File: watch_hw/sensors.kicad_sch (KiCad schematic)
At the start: 4 parts, among them J2 FH19C-7S-0.5SH, U7 BMA456

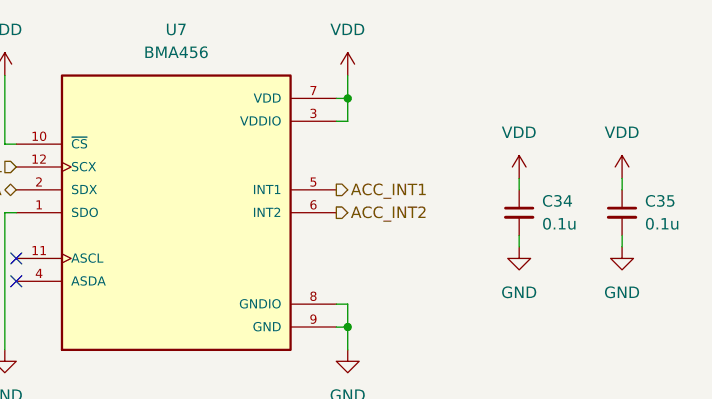
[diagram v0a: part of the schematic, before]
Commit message: Finalize (?) part selection, start layout
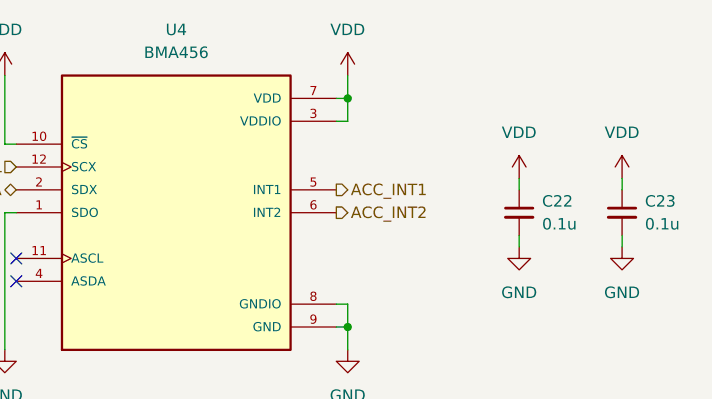
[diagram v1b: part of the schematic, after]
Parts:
- renumbered C34 to C22, C35 to C23, U7 to U4

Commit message: Routing progress
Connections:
- net HR_GPIO: no longer names the net of J2.3 (Pin_3)
- net HR_LDO_EN: no longer names the net of J2.4 (Pin_4)
- no-connect marks 2 -> 4
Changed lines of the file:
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@@
   (junction (at 220.98 107.95) (diameter 0) (color 0 0 0 0)
   )
+  (no_connect (at 81.28 92.71))
   (no_connect (at 184.15 100.33))
   (no_connect (at 184.15 102.87))
+  (no_connect (at 81.28 90.17))
   (wire (pts (xy 219.71 82.55) (xy 220.98 82.55))
     (stroke (width 0) (type default))
@@
     (effects (font (size 1.27 1.27)) (justify right))
   )
-  (hierarchical_label "HR_GPIO" (shape bidirectional) (at 81.28 90.17 180) (fields_autoplaced)
-    (effects (font (size 1.27 1.27)) (justify right))
-  )
   (hierarchical_label "HR_INT" (shape output) (at 81.28 87.63 180) (fields_autoplaced)
     (effects (font (size 1.27 1.27)) (justify right))
@@
     (effects (font (size 1.27 1.27)) (justify right))
   )
-  (hierarchical_label "HR_LDO_EN" (shape input) (at 81.28 92.71 180) (fields_autoplaced)
-    (effects (font (size 1.27 1.27)) (justify right))
-  )

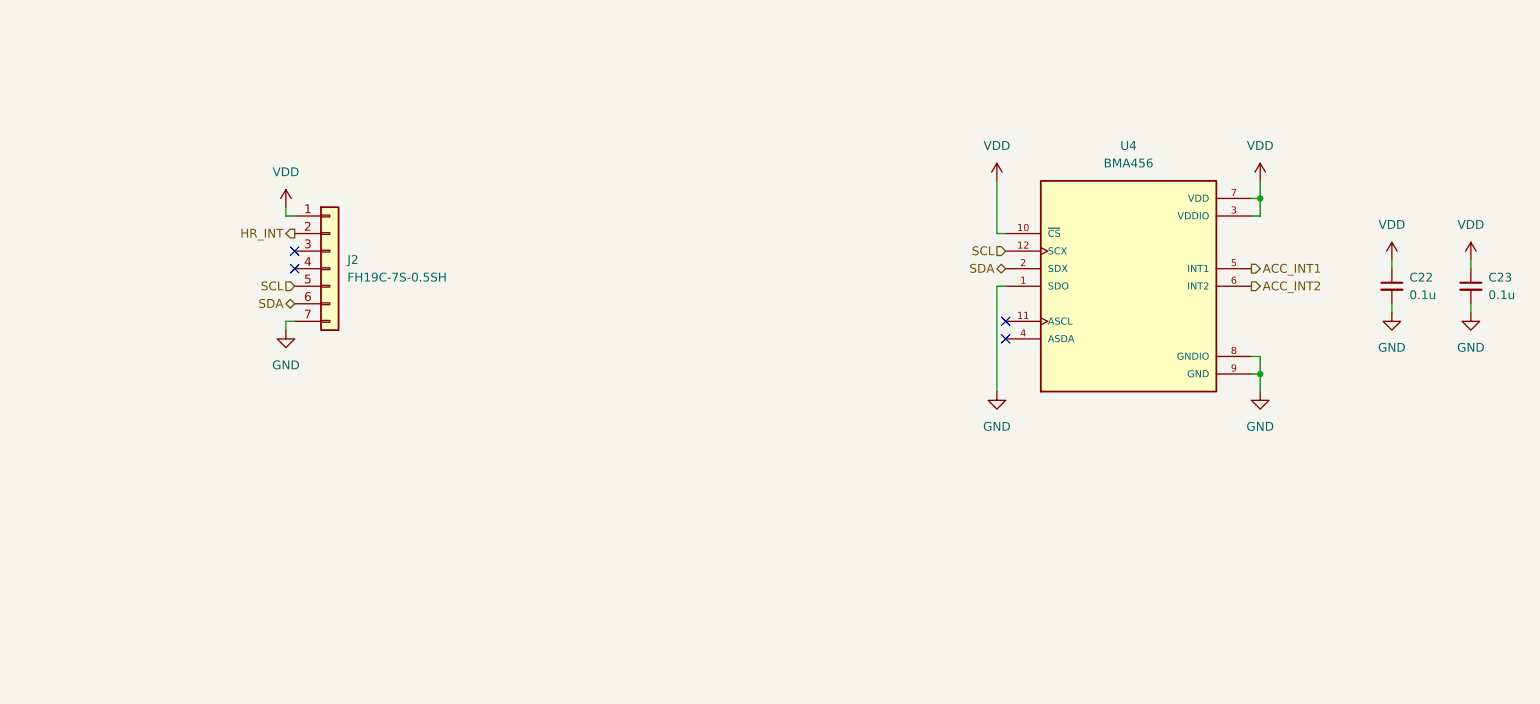
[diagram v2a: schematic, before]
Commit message: Clean up library symbols, update to kicad 8
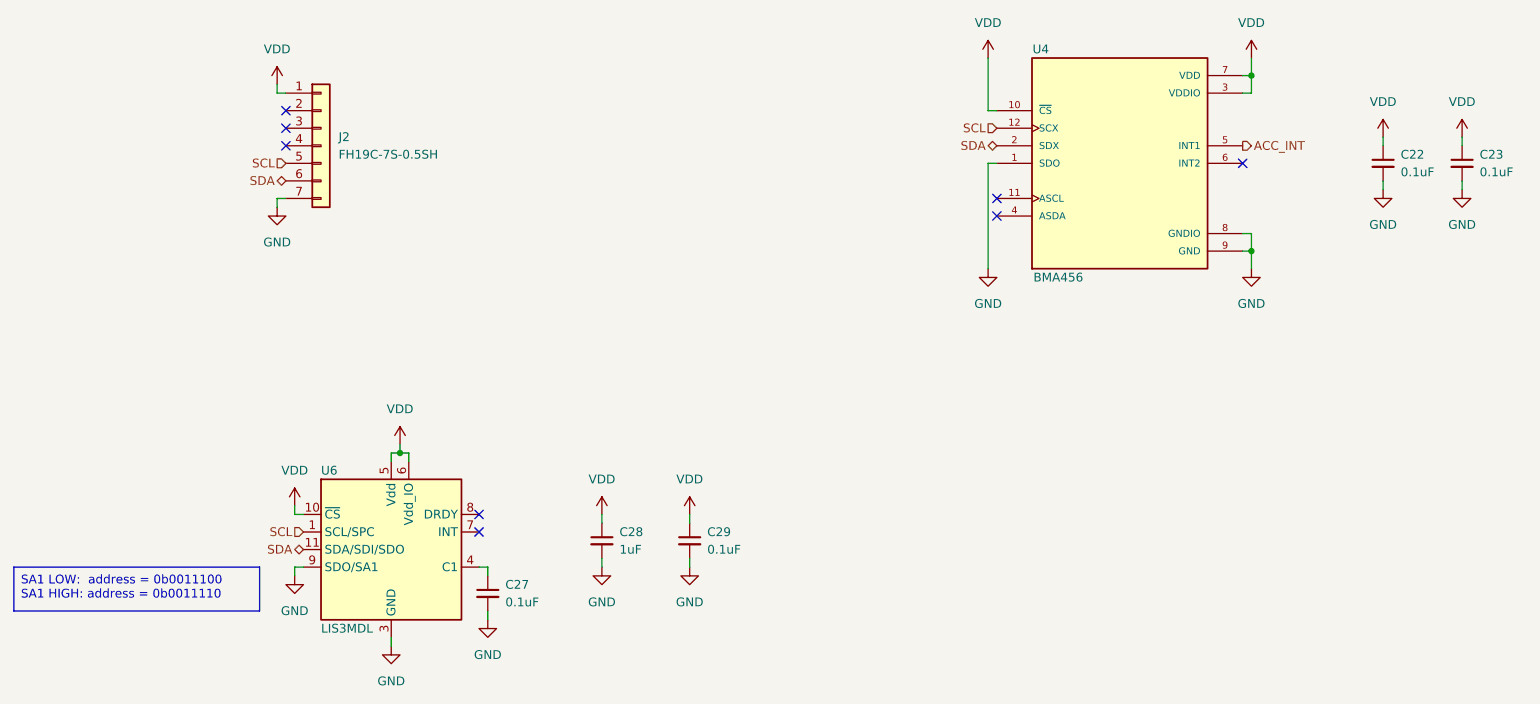
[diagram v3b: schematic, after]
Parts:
- added C27, C29: 0.1uF, Capacitor_SMD:C_0402_1005Metric_Pad0.74x0.62mm_HandSolder, symbol Device:C_Small
- added C28: 1uF, Capacitor_SMD:C_0402_1005Metric_Pad0.74x0.62mm_HandSolder, symbol Device:C_Small
- added U6: LIS3MDL, watch:LIS3MDLTR, symbol Sensor_Magnetic:LIS3MDL
- C22, C23: value 0.1u -> 0.1uF
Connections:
- net GND: now also C27.2, C28.2, C29.2, U6.12 (GND), U6.2 (GND), U6.3 (GND), U6.9 (SDO/SA1)
- net SCL: now also U6.1 (SCL/SPC)
- net SDA: now also U6.11 (SDA/SDI/SDO)
- net VDD: now also C28.1, C29.1, U6.10 (~{CS}), U6.5 (Vdd), U6.6 (Vdd_IO)
- net ACC_INT1 renamed ACC_INT
- net ACC_INT2: no longer names the net of U4.6 (INT2)
- net HR_INT: no longer names the net of J2.2 (Pin_2)
- new net: C27.1, U6.4 (C1)
- no-connect marks 4 -> 8
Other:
- moved on the sheet: C22, C23, J2, U4

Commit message: Start watch v1 layout
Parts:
- removed C27, C29: 0.1uF, Capacitor_SMD:C_0402_1005Metric_Pad0.74x0.62mm_HandSolder, symbol Device:C_Small
- removed C28: 1uF, Capacitor_SMD:C_0402_1005Metric_Pad0.74x0.62mm_HandSolder, symbol Device:C_Small
- removed U6: LIS3MDL, watch:LIS3MDLTR, symbol Sensor_Magnetic:LIS3MDL
- J2: value FH19C-7S-0.5SH -> FH19C-7S-0.5SH(10)
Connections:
- no-connect marks 8 -> 6

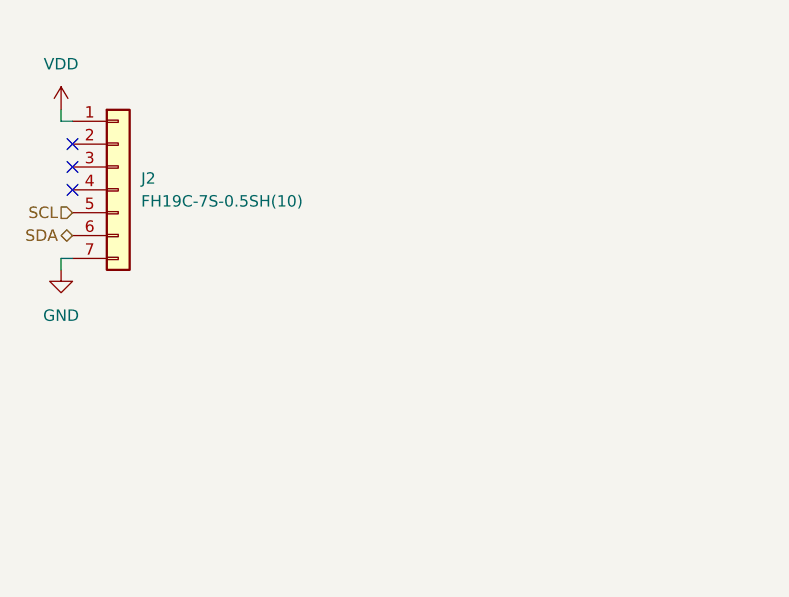
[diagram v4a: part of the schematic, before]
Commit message: Add pulse sensor straight to board, fix NPM1100 symbol/footprint
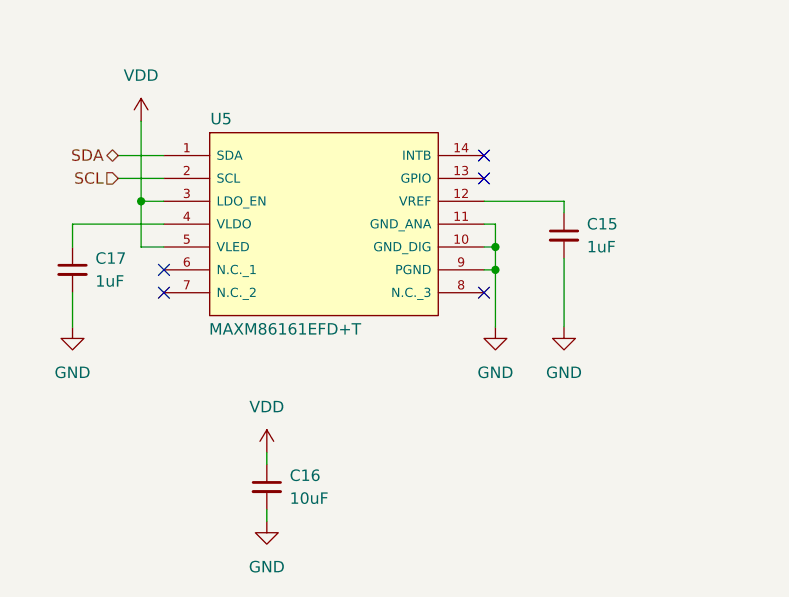
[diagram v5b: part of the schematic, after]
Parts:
- removed J2: FH19C-7S-0.5SH(10), watch:FH19C-7S-0.5SH, symbol Connector_Generic:Conn_01x07
- added C15, C17: 1uF, Capacitor_SMD:C_0402_1005Metric_Pad0.74x0.62mm_HandSolder, symbol Device:C_Small
- added C16: 10uF, Capacitor_SMD:C_0805_2012Metric_Pad1.18x1.45mm_HandSolder, symbol Device:C_Small
- added U5: MAXM86161EFD+T, watch:MAXM86161EFDT, symbol watch:MAXM86161EFD+T
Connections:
- net GND: now also C15.2, C16.2, C17.2, U5.10 (GND_DIG), U5.11 (GND_ANA), U5.9 (PGND)
- net SCL: now also U5.2 (SCL)
- net SDA: now also U5.1 (SDA)
- net VDD: now also C16.1, U5.3 (LDO_EN), U5.5 (VLED)
- new net: C15.1, U5.12 (VREF)
- new net: C17.1, U5.4 (VLDO)
- no-connect marks 6 -> 8

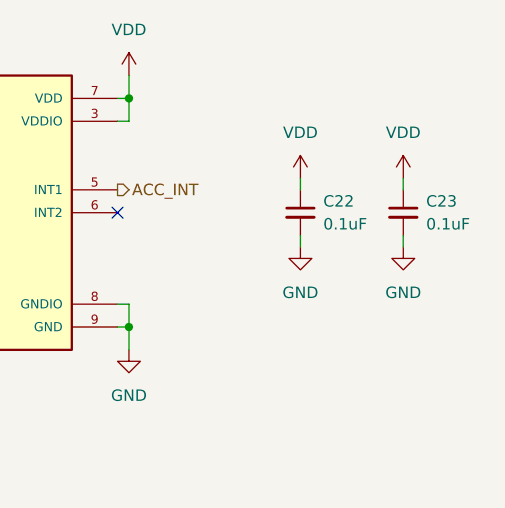
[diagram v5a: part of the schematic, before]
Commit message: Add manufacturer/PN fields, select LCSC parts
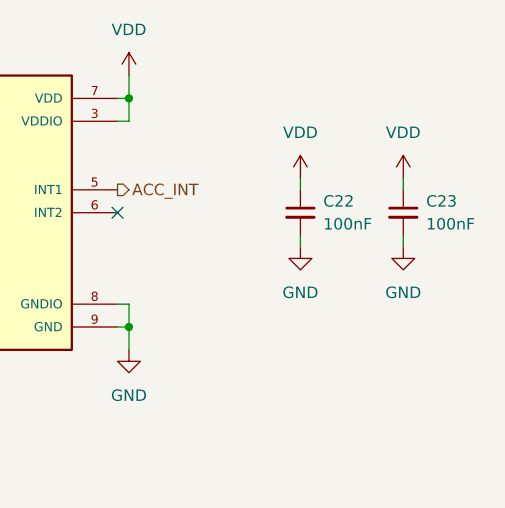
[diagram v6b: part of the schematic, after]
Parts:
- C15, C17: LCSC (none) -> C52923
- C16: LCSC (none) -> C15850
- C22, C23: value 0.1uF -> 100nF; LCSC (none) -> C1525
- U4: LCSC (none) -> C189518
- U5: LCSC (none) -> C3178309
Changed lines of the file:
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@@
 			)
 		)
-		(property "Value" "0.1uF"
+		(property "Value" "100nF"
 			(at 241.3 78.7462 0)
 			(effects
@@
 		)
 		(property "Description" ""
+			(at 238.76 77.47 0)
+			(effects
+				(font
+					(size 1.27 1.27)
+				)
+				(hide yes)
+			)
+		)
+		(property "LCSC" "C1525"
 			(at 238.76 77.47 0)
 			(effects
@@
 			)
 		)
+		(property "LCSC" "C189518"
+			(at 200.66 77.47 0)
+			(effects
+				(font
+					(size 1.27 1.27)
+				)
+				(hide yes)
+			)
+		)
 		(pin "1"
 		)
@@
 			)
 		)
+		(property "LCSC" "C52923"
+			(at 134.62 80.01 0)
+			(effects
+				(font
+					(size 1.27 1.27)
+				)
+				(hide yes)
+			)
+		)
 		(pin "1"
 		)
@@
 			)
 		)
-		(property "Value" "0.1uF"
+		(property "Value" "100nF"
 			(at 252.73 78.7462 0)
 			(effects
@@
 		)
 		(property "Description" ""
+			(at 250.19 77.47 0)
+			(effects
+				(font
+					(size 1.27 1.27)
+				)
+				(hide yes)
+			)
+		)
+		(property "LCSC" "C1525"
 			(at 250.19 77.47 0)
 			(effects
@@
 			)
 		)
+		(property "LCSC" "C3178309"
+			(at 90.17 71.12 0)
+			(effects
+				(font
+					(size 1.27 1.27)
+				)
+				(hide yes)
+			)
+		)
 		(pin "4"
 		)
@@
 			)
 		)
+		(property "LCSC" "C52923"
+			(at 80.01 83.82 0)
+			(effects
+				(font
+					(size 1.27 1.27)
+				)
+				(hide yes)
+			)
+		)
 		(pin "1"
 		)
@@
 			(at 101.6 107.95 0)
 			(effects
+				(font
+					(size 1.27 1.27)
+				)
+				(hide yes)
+			)
+		)
+		(property "LCSC" "C15850"
+			(at 101.6 107.95 0)
+			(effects

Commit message: Finish adding MPN info
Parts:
- C15, C17: Manufacturer (none) -> Samsung; Manufacturer Part Number (none) -> CL05A105KA5NQNC
- C16: Manufacturer (none) -> Samsung; Manufacturer Part Number (none) -> CL21A106KAYNNNE
- C22, C23: Manufacturer (none) -> Samsung; Manufacturer Part Number (none) -> CL05B104KO5NNNC
- U4: Manufacturer (none) -> Bosch; Manufacturer Part Number (none) -> BMA456
- U5: Manufacturer Part Number (none) -> MAXM86161EFD+T
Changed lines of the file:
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@@
+			)
+		)
+		(property "Manufacturer" "Samsung"
+			(at 238.76 77.47 0)
+			(effects
+				(font
+					(size 1.27 1.27)
+				)
+				(hide yes)
+			)
+		)
+		(property "Manufacturer Part Number" "CL05B104KO5NNNC"
+			(at 238.76 77.47 0)
+			(effects
+				(font
+					(size 1.27 1.27)
+				)
+				(hide yes)
 			)
 		)
@@
 			)
 		)
+		(property "Manufacturer" "Bosch"
+			(at 200.66 77.47 0)
+			(effects
+				(font
+					(size 1.27 1.27)
+				)
+				(hide yes)
+			)
+		)
+		(property "Manufacturer Part Number" "BMA456"
+			(at 200.66 77.47 0)
+			(effects
+				(font
+					(size 1.27 1.27)
+				)
+				(hide yes)
+			)
+		)
 		(pin "1"
 		)
@@
 			)
 		)
+		(property "Manufacturer" "Samsung"
+			(at 134.62 80.01 0)
+			(effects
+				(font
+					(size 1.27 1.27)
+				)
+				(hide yes)
+			)
+		)
+		(property "Manufacturer Part Number" "CL05A105KA5NQNC"
+			(at 134.62 80.01 0)
+			(effects
+				(font
+					(size 1.27 1.27)
+				)
+				(hide yes)
+			)
+		)
 		(pin "1"
 		)
@@
 			)
 		)
+		(property "Manufacturer" "Samsung"
+			(at 250.19 77.47 0)
+			(effects
+				(font
+					(size 1.27 1.27)
+				)
+				(hide yes)
+			)
+		)
+		(property "Manufacturer Part Number" "CL05B104KO5NNNC"
+			(at 250.19 77.47 0)
+			(effects
+				(font
+					(size 1.27 1.27)
+				)
+				(hide yes)
+			)
+		)
 		(pin "1"
 		)
@@
 			)
 		)
+		(property "Manufacturer Part Number" "MAXM86161EFD+T"
+			(at 90.17 71.12 0)
+			(effects
+				(font
+					(size 1.27 1.27)
+				)
+				(hide yes)
+			)
+		)
 		(pin "4"
 		)
@@
 			)
 		)
+		(property "Manufacturer" "Samsung"
+			(at 80.01 83.82 0)
+			(effects
+				(font
+					(size 1.27 1.27)
+				)
+				(hide yes)
+			)
+		)
+		(property "Manufacturer Part Number" "CL05A105KA5NQNC"
+			(at 80.01 83.82 0)
+			(effects
+				(font
+					(size 1.27 1.27)
+				)
+				(hide yes)
+			)
+		)
 		(pin "1"
 		)
@@
 			(at 101.6 107.95 0)
 			(effects
+				(font
+					(size 1.27 1.27)
+				)
+				(hide yes)
+			)
+		)
+		(property "Manufacturer" "Samsung"
+			(at 101.6 107.95 0)
+			(effects
+				(font
+					(size 1.27 1.27)
+				)
+				(hide yes)
+			)
+		)
+		(property "Manufacturer Part Number" "CL21A106KAYNNNE"
+			(at 101.6 107.95 0)
+			(effects
